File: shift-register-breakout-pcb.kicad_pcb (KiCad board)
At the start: 2 copper layers, 70 x 40 mm, 19 parts, among them J1 Conn_01x07_Socket, J2 Conn_01x08_Socket, J3 Conn_01x08_Socket, J4 Conn_01x08_Socket, J5 Conn_01x08_Socket

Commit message: adding text, fixing some errors.
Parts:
- added LOGO1: **REF, ct-kicad:awesome-logo, F.Cu at (75.1, 77.4)
- added LOGO2: **REF, ct-kicad:qmk-lite, F.Cu at (137.1, 70.1)
- added LOGO3: **REF, ct-kicad:qmk-lite, B.Cu at (137.2, 70.2)
- added LOGO4: **REF, ct-kicad:awesome-logo, B.Cu at (75.1, 77.5)
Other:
- board text added: "COL2 589 REGISTERS COL1"
- board text added: "Col0"
- board text added: "Col15"
- board text added: "ROW1 595 REGISTERS ROW2"
- board text added: "Row0"
- board text added: "Row15"
- board text added: "v1.0"

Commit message: fixing mosfet notes in schematic as per burkfers, final pcb notation added
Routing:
- net GND: vias 64 -> 71
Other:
- board text added: "3V3"
- board text added: "CLK"
- board text added: "COL"
- board text added: "DIODE: ROW2COL"
- board text added: "GND"
- board text added: "MISO"
- board text added: "READ"
- board text added: "ROW"
- board text added: "WRITE"

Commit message: updating readme with details
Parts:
- moved LOGO1 1.50 mm to (76.2, 78.4)
- moved LOGO4 1.45 mm to (76.2, 78.4)
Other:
- board text added: "Hole: M3"
- board text added: "MATRIX-INATOR"

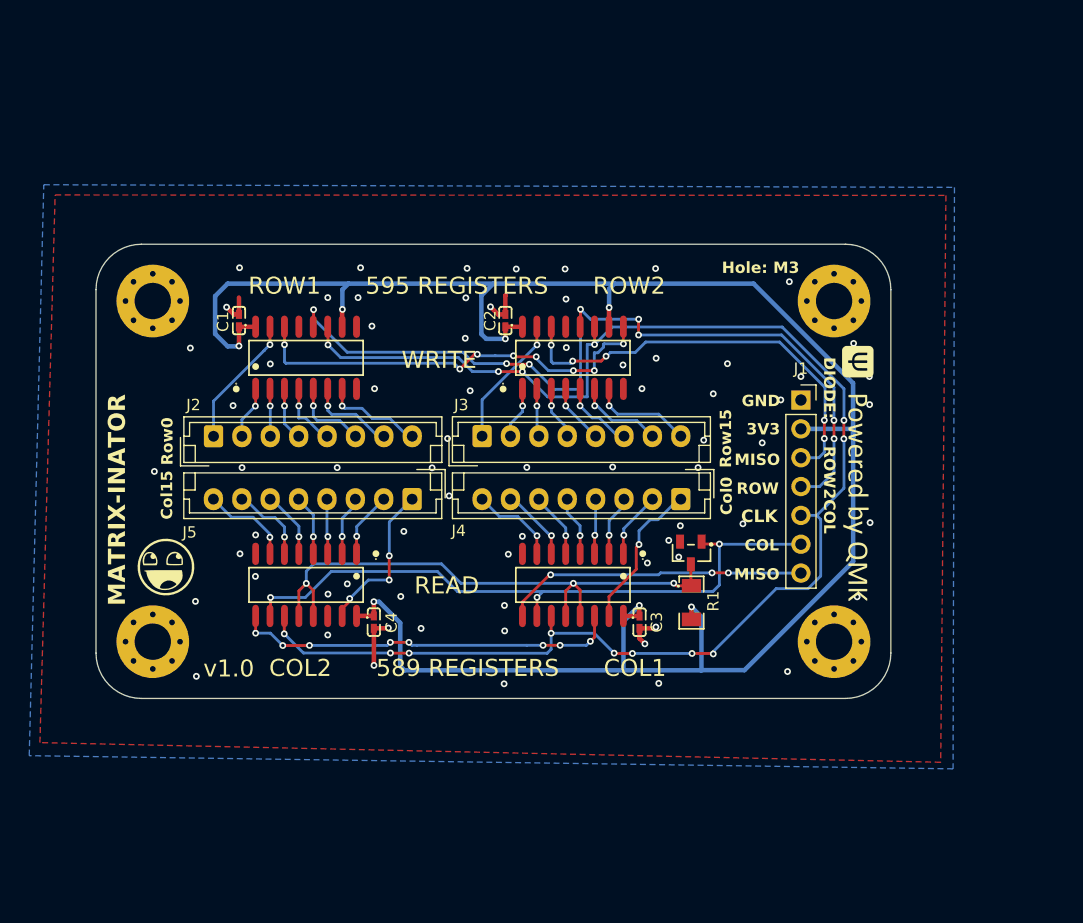
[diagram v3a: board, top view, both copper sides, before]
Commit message: adding latch circuit and resistor arrays
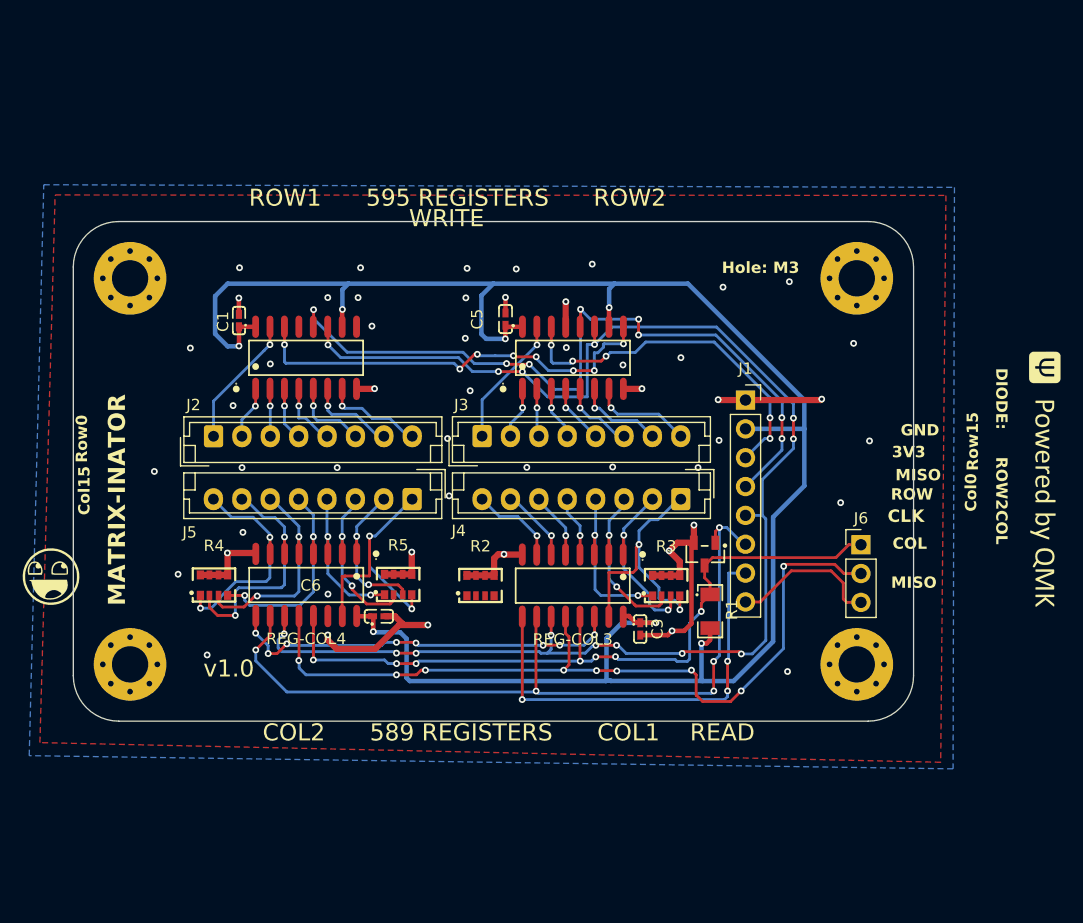
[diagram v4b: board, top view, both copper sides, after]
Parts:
- removed C2, C4: 100nF, ct-kicad:C0402
- removed REG-COL1, REG-COL2: MC74HC589ADR2G, ct-kicad:SOIC-16_L9.9-W3.9-P1.27-LS6.0-BL
- added C5: 100nF, ct-kicad:C0402, F.Cu at (106.1, 56.6)
- added C6: 100nF, ct-kicad:C0402, F.Cu at (94.9, 82.8)
- added J6: Conn_01x03_Socket, Connector_PinHeader_2.54mm:PinHeader_1x03_P2.54mm_Vertical, F.Cu at (137.4, 76.5)
- added R2: 4D03WGJ0103T5E, ct-kicad:RES-ARRAY-SMD_0603-8P-L3.2-W1.6-BL, F.Cu at (103.9, 80.1)
- added R3: 4D03WGJ0103T5E, ct-kicad:RES-ARRAY-SMD_0603-8P-L3.2-W1.6-BL, F.Cu at (120.2, 80.1)
- added R4: 4D03WGJ0103T5E, ct-kicad:RES-ARRAY-SMD_0603-8P-L3.2-W1.6-BL, F.Cu at (80.4, 80.0)
- added R5: 4D03WGJ0103T5E, ct-kicad:RES-ARRAY-SMD_0603-8P-L3.2-W1.6-BL, F.Cu at (96.6, 80.0)
- added REG-COL3: MC74HC589ADR2G, ct-kicad:SOIC-16_L9.9-W3.9-P1.27-LS6.0-BL, F.Cu at (112.0, 80.1)
- added REG-COL4: MC74HC589ADR2G, ct-kicad:SOIC-16_L9.9-W3.9-P1.27-LS6.0-BL, F.Cu at (88.5, 80.0)
- J1: value Conn_01x07_Socket -> Conn_01x08_Socket; footprint Connector_PinSocket_2.54mm:PinSocket_1x07_P2.54mm_Vertical -> Connector_PinSocket_2.54mm:PinSocket_1x08_P2.54mm_Vertical
- moved LOGO2 16.5 mm to (153.6, 70.6)
- moved LOGO1 10.2 mm to (66.0, 79.3)
- moved J1 4.88 mm to (127.2, 63.7)
- moved H1 2.83 mm to (73.0, 53.0)
- moved H2 2.83 mm to (137.0, 53.0)
- moved H3 2.83 mm to (73.0, 87.0)
- moved H4 2.83 mm to (137.0, 87.0)
- moved R1 1.81 mm to (124.1, 82.3)
- moved COL_CS_MOS1 1.22 mm to (123.6, 77.3)
- moved C3 0.60 mm to (117.9, 83.9)
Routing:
- net Net-(J6-Pin_2): track 0.00 -> 71.4 mm, vias 0 -> 9
- net GND: track 13.7 -> 68.9 mm, vias 71 -> 51
- net Net-(REG-COL3-SA): track 0.00 -> 35.2 mm, vias 0 -> 8
- net Net-(REG-COL1-SA): track 34.2 -> 0.00 mm, vias 8 -> 0
- net COL_CS_MOS: track 50.5 -> 65.3 mm, vias 3 -> 7
- net col14: track 7.14 -> 21.7 mm, vias 1 -> 2
- net COL_CS: track 57.9 -> 71.7 mm, vias 3 -> 5
- net col12: track 5.35 -> 18.9 mm, vias 1 -> 2
- net COL_LATCH: track 0.00 -> 13.4 mm
- net col13: track 5.95 -> 19.2 mm, vias 1 -> 2
- net col15: track 7.99 -> 20.0 mm, vias 1 -> 2
- net SPI_MISO: track 26.8 -> 37.9 mm
- net col0: track 13.4 -> 23.8 mm, vias 1 -> 2
- net col1: track 5.87 -> 16.1 mm, vias 1 -> 2
- net col2: track 5.36 -> 15.6 mm, vias 1 -> 2
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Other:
- board size 70 x 40 mm -> 74 x 44 mm

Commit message: some silkscreen and other changes
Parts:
- moved LOGO2 80.7 mm to (72.9, 70.5), turned to 90 degrees
- moved LOGO1 69.3 mm to (130.6, 54.0)
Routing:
- net COL_CS: track 71.7 -> 69.8 mm
- net Net-(REG-COL3-SA): track 35.2 -> 36.1 mm
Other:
- board text added: "C.CS"
- board text added: "Cl.0"
- board text added: "Cl.15"
- board text added: "L"
- board text added: "LATCH"
- board text added: "MOSI"
- board text added: "R.CS"
- board text added: "Rw.0"
- board text added: "Rw.15"
- board text added: "v1.1"
- board text removed: "COL"
- board text removed: "COL2 589 REGISTERS COL1"
- board text removed: "Col0"
- board text removed: "Col15"
- board text removed: "READ"
- board text removed: "ROW"
- board text removed: "ROW1 595 REGISTERS ROW2"
- board text removed: "Row0"
- board text removed: "Row15"
- board text removed: "WRITE"

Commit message: vik-i-fying the design
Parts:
- removed H2, H3, H4: MountingHole, MountingHole:MountingHole_3.2mm_M3_Pad_Via
- added FID1: Fiducial, vik:vik-logo-small, F.Cu at (121.8, 98.2)
- added J7: vik-module-connector, ct-kicad:FPC-SMD_XF2M-1215-1AH, F.Cu at (132.6, 55.7)
- H1: footprint MountingHole:MountingHole_3.2mm_M3_Pad_Via -> vik:vik-module-mounting-large
- J6: moved to B.Cu
- moved LOGO2 44.5 mm to (106.4, 99.8), turned to 0 degrees
- moved J6 39.0 mm to (100.9, 90.4), turned to -90 degrees
- moved H1 38.0 mm to (106.6, 70.6)
- moved LOGO1 12.0 mm to (134.6, 42.6)
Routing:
- net COL_LATCH: track 13.4 -> 64.5 mm, vias 0 -> 6
- net GND: track 68.9 -> 104.7 mm
- net +3V3: track 171.3 -> 206.1 mm, vias 7 -> 12
- net SPI_MISO: track 37.9 -> 69.1 mm, vias 3 -> 7
- net Net-(J6-Pin_2): track 71.4 -> 43.3 mm, vias 9 -> 4
- net COL_CS: track 69.8 -> 93.3 mm, vias 5 -> 11
- net SPI_MOSI: track 31.6 -> 47.1 mm, vias 5 -> 8
- net ROW_CS: track 67.8 -> 80.3 mm, vias 8 -> 10
- net COL_CS_MOS: track 65.3 -> 55.3 mm, vias 7 -> 5
- net SPI_CLK: track 128.7 -> 138.5 mm, vias 14 -> 13
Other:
- board size 74 x 44 mm -> 64.9 x 65 mm
- board text added: "COLS"
- board text added: "COL_CS JOIN"
- board text added: "Hole: M2"
- board text added: "LATCH ENABLE"
- board text added: "ROWS"
- board text removed: "Hole: M3"
- board text removed: "L"

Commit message: has been suggested to minimize the design...
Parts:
- removed LOGO2: **REF, ct-kicad:qmk-lite
- moved FID1 42.5 mm to (124.3, 55.9)
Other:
- board text added: "VIK"

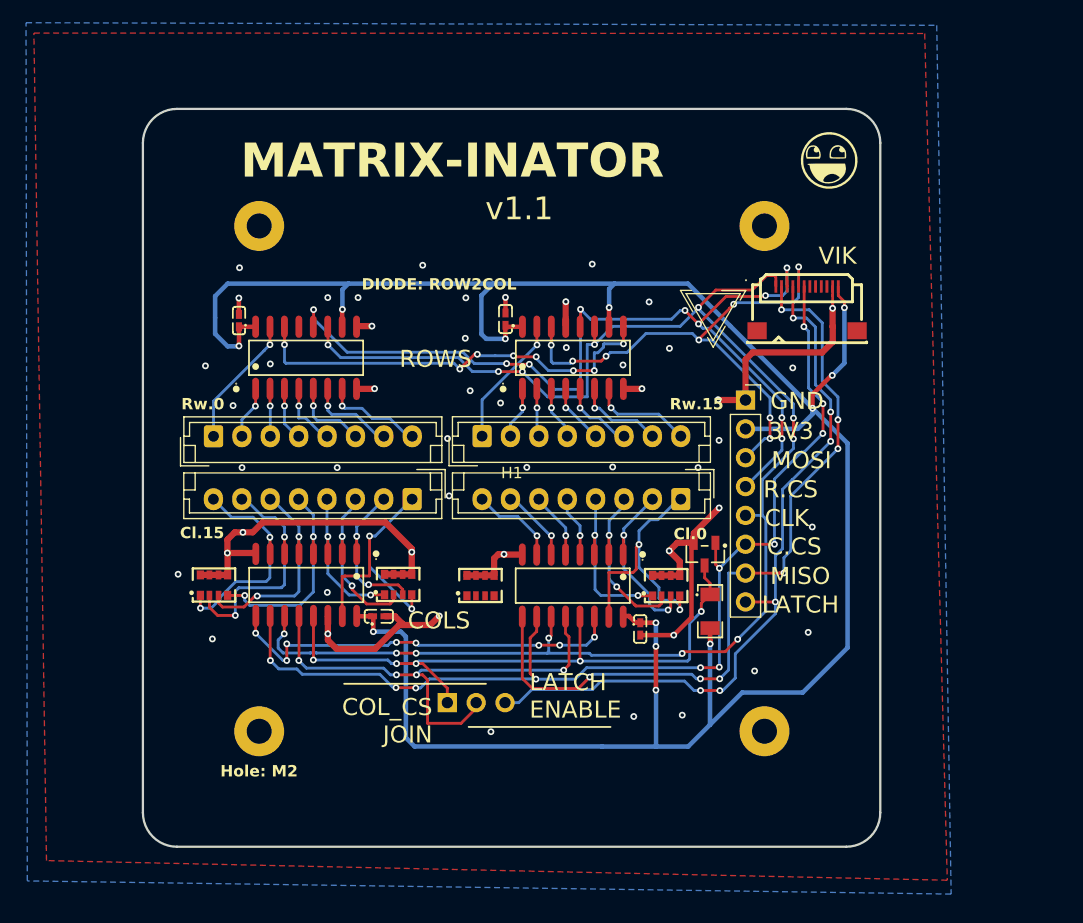
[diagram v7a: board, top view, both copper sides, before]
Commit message: mostly done vik-ifying it
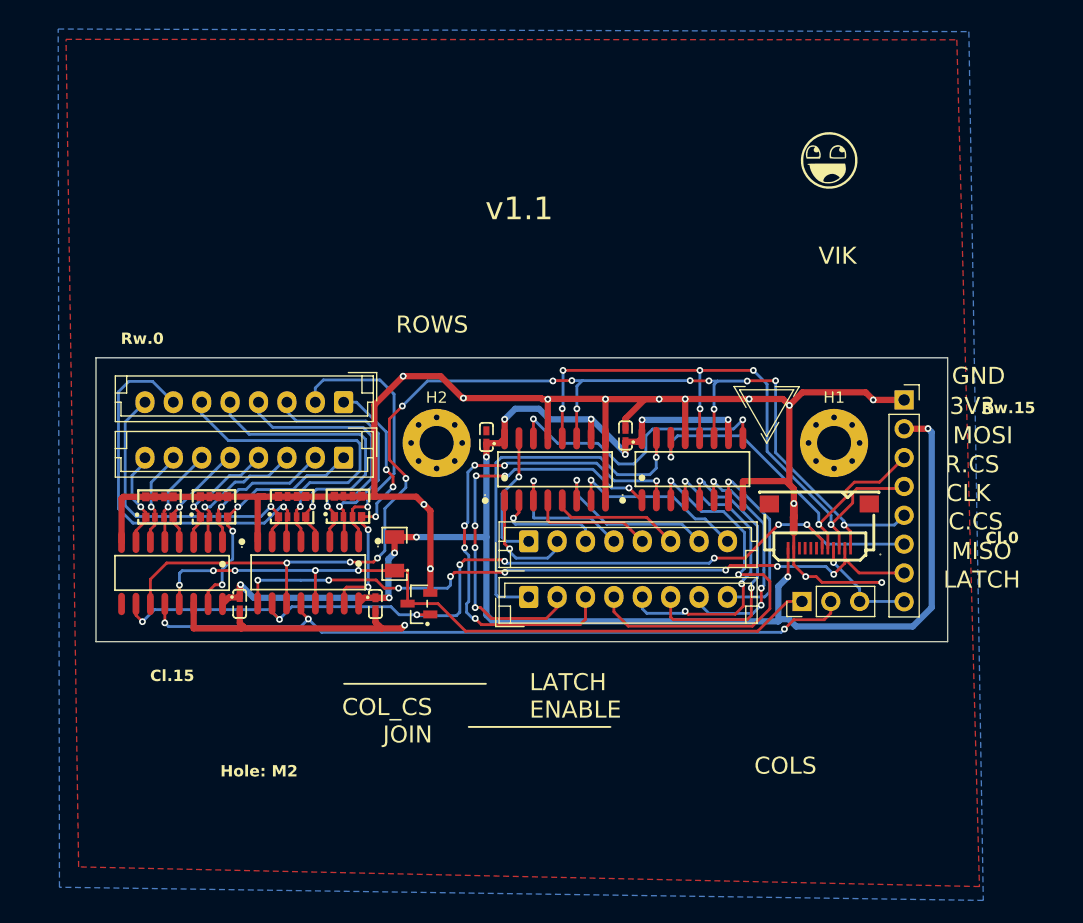
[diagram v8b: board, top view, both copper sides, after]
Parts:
- added H2: MountingHole, MountingHole:MountingHole_3mm_Pad_Via, F.Cu at (100.0, 67.5)
- H1: footprint vik:vik-module-mounting-large -> MountingHole:MountingHole_3mm_Pad_Via
- J6: moved to F.Cu
- moved C5 34.3 mm to (82.7, 81.7), turned to -90 degrees
- moved J6 32.5 mm to (132.2, 81.5), turned to 90 degrees
- moved J4 30.9 mm to (91.8, 63.9)
- moved J2 29.3 mm to (108.1, 76.2)
- moved R3 28.9 mm to (92.2, 73.1)
- moved H1 28.6 mm to (135.0, 67.5)
- moved R1 28.2 mm to (96.3, 77.3), turned to 90 degrees
- moved LOGO3 26.8 mm to (149.5, 94.0)
- moved COL_CS_MOS1 25.5 mm to (98.4, 81.6), turned to 0 degrees
- moved C1 24.1 mm to (104.4, 67.0)
- moved REG-ROW1 24.0 mm to (110.4, 69.8)
- moved REG-COL3 23.3 mm to (88.7, 78.9)
- moved J7 19.2 mm to (133.7, 74.8), turned to 180 degrees
- moved R2 18.0 mm to (87.3, 73.1)
- moved R5 17.6 mm to (80.4, 73.1)
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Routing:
- net GND: track 104.7 -> 175.0 mm, vias 51 -> 15
- net +3V3: track 206.1 -> 145.0 mm
- net COL_LATCH: track 64.5 -> 9.58 mm, vias 6 -> 1
- net row10: track 4.24 -> 45.1 mm, vias 1 -> 6
- net Net-(REG-COL3-SA): track 36.3 -> 0.00 mm, vias 8 -> 0
- net row9: track 4.61 -> 36.6 mm, vias 1 -> 6
- net row11: track 4.75 -> 35.6 mm, vias 1 -> 2
- net SPI_CLK: track 138.5 -> 109.4 mm, vias 13 -> 14
- net col6: track 6.55 -> 35.1 mm
- net ROW_CS: track 80.3 -> 55.9 mm, vias 10 -> 6
- net col5: track 5.80 -> 29.1 mm
- net col4: track 5.28 -> 27.2 mm
- net row12: track 5.34 -> 27.0 mm, vias 1 -> 3
- net Net-(J6-Pin_2): track 43.3 -> 64.6 mm, vias 4 -> 3
- net row8: track 11.6 -> 32.4 mm
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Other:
- board size 64.9 x 65 mm -> 75 x 25 mm
